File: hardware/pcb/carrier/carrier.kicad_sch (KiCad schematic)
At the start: 34 parts

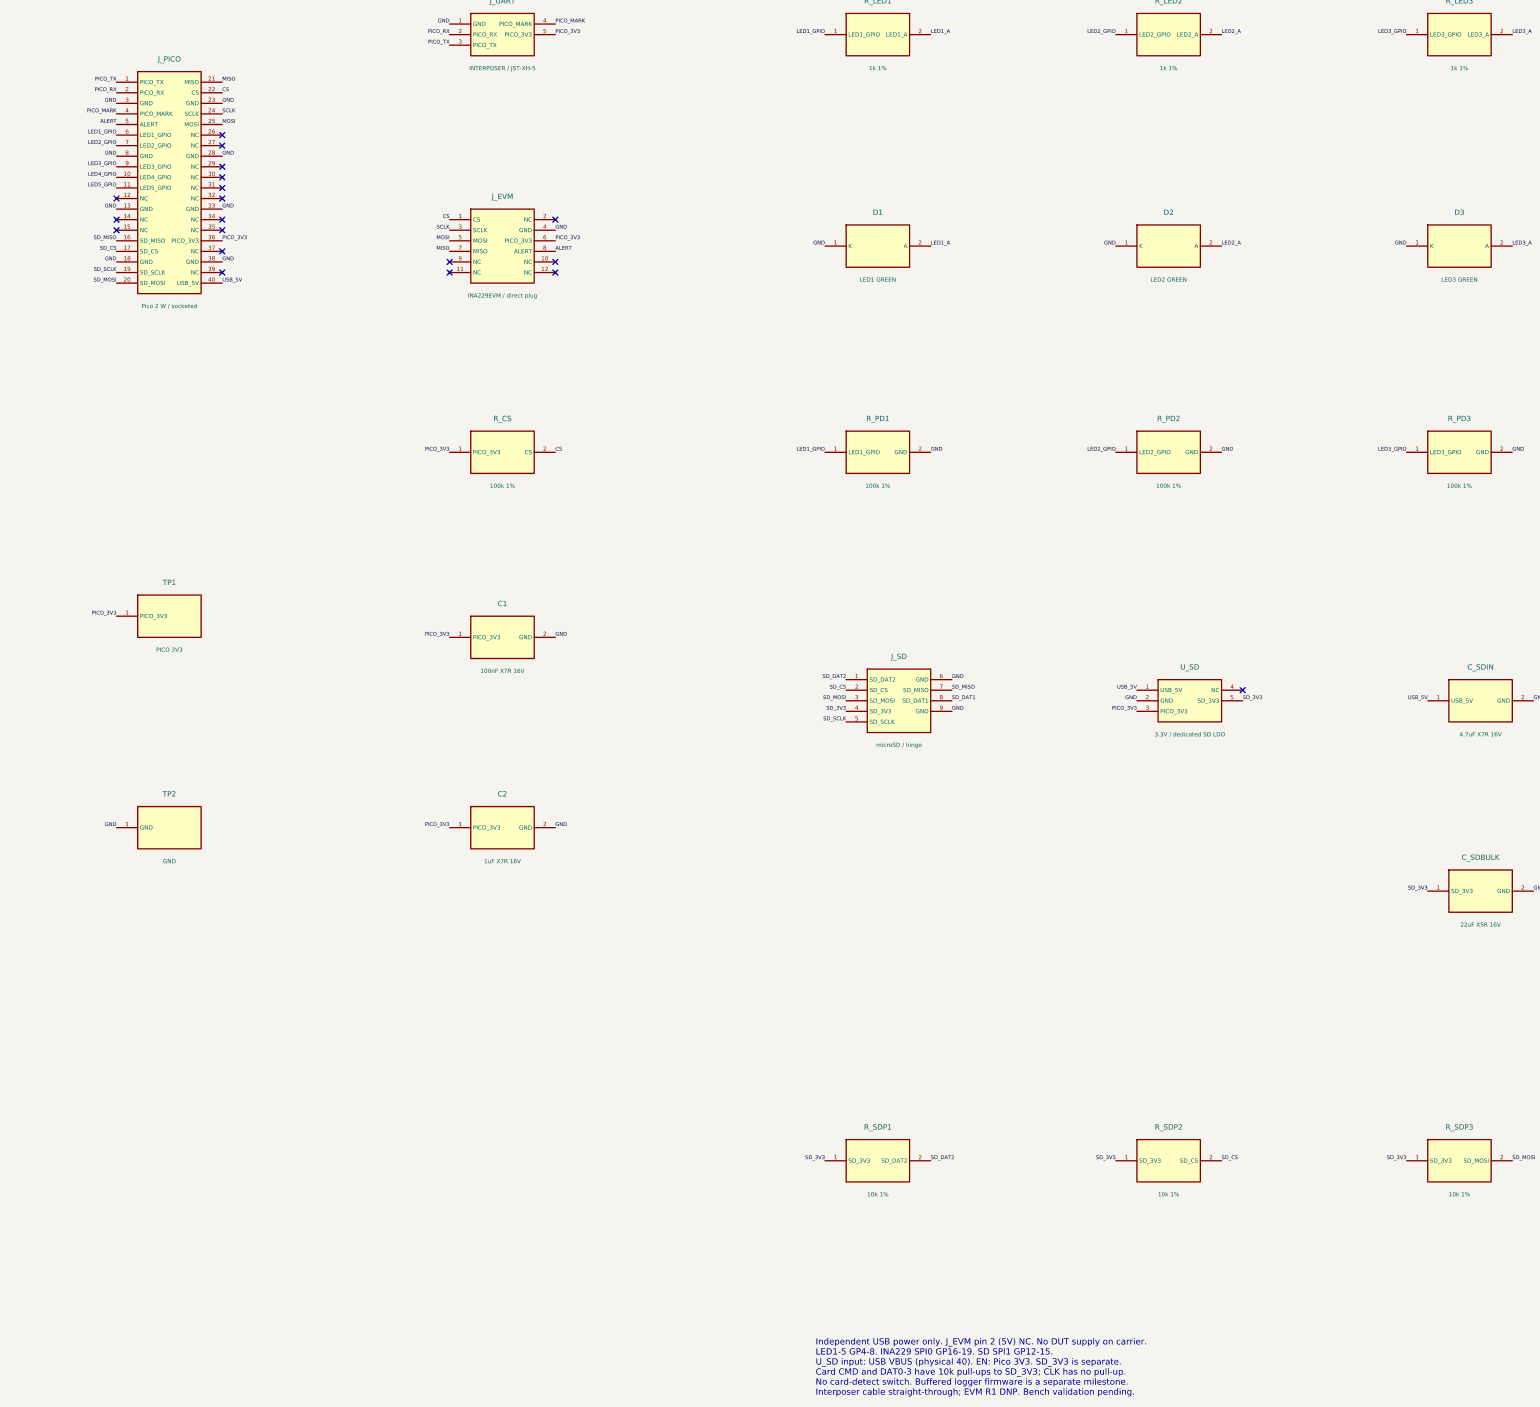
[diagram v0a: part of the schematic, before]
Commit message: Replace INA229EVM with an on-board INA229 on the carrier
- Carrier carries U_PM (INA229AIDGSR, VSSOP-10), 100 nF bypass, ALERT
  pull-up and a JST-XH sense connector J_SENSE (same pinout as interposer
  J3); the EVM socket and its footprint are removed.
- Carrier outline grows from 66 to 78 x 54 mm to make room.
- INA229 SPI0 moves to GP4-GP7 and the LEDs to GP27/26/22/21/20 so no
  trace crosses the Pico; ALERT stays on GP3.
- Carrier PWR_FLAGs added; source checks and tests updated for the new
  measurement boundary (sense nets only on J_SENSE and U_PM).
- BOM, assembly review, passive selections, checklist (new sense-ic row,
  carrier mock-up reset to pending), footprint review and docs updated.
- INA229 pad geometry compared with the TI DGS0010A example land pattern.
- Add project-state handoff note. Interposer and carrier fabrication
  gates remain open; nothing is released.

make carrier-build does not currently reproduce the routed board; the saved
carrier.kicad_pcb is the source of truth (see the carrier README).

Co-Authored-By: Claude Sonnet 5.5 <noreply@anthropic.com>
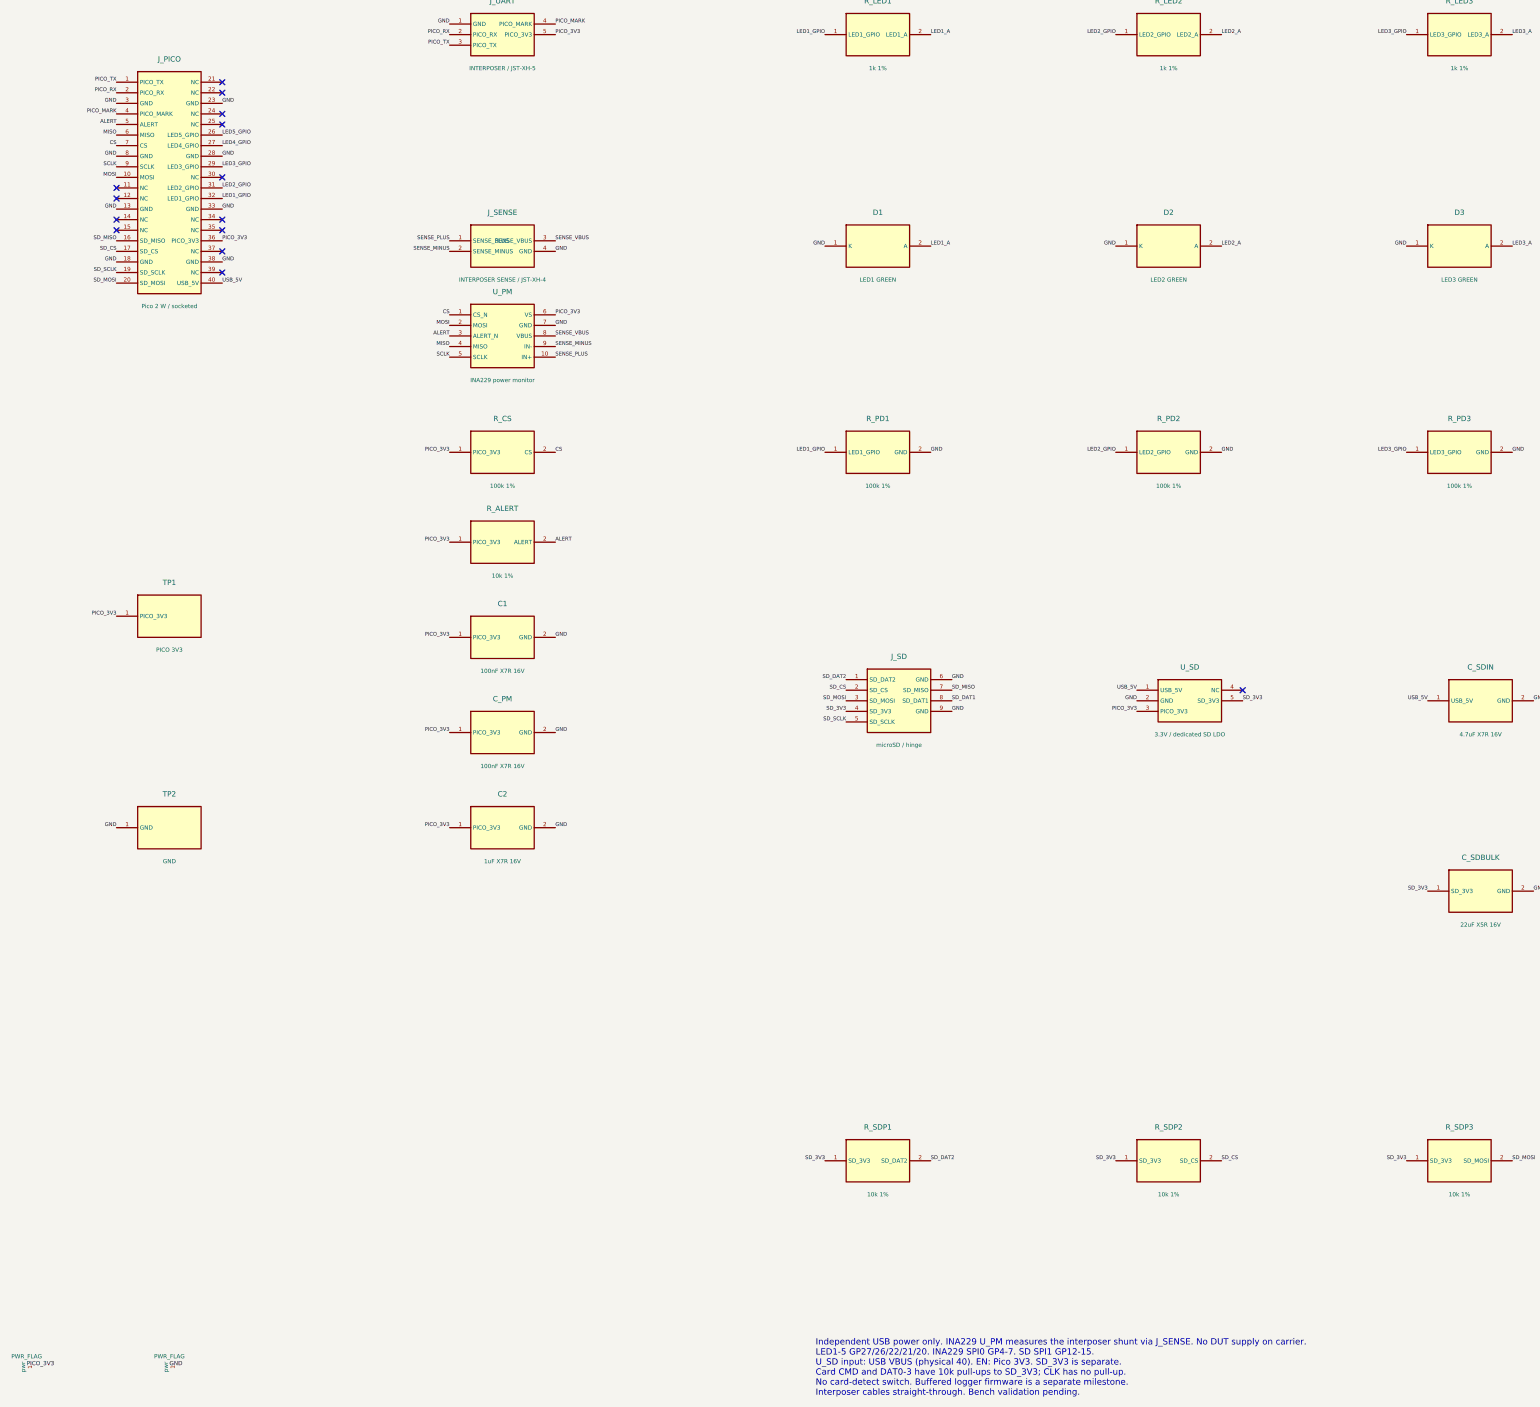
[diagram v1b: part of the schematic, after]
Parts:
- removed J_EVM: INA229EVM / direct plug, Carrier:NPPN062FJFN, symbol Carrier:J_EVM
- added C_PM: 100nF X7R 16V, Carrier:C_0805_Murata, symbol Carrier:C_PM
- added J_SENSE: INTERPOSER SENSE / JST-XH-4, Carrier:XH4, symbol Carrier:J_SENSE
- added R_ALERT: 10k 1%, Carrier:R_0805, symbol Carrier:R_ALERT
- added U_PM: INA229 power monitor, Carrier:VSSOP10, symbol Carrier:U_PM
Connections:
- net ALERT: now also R_ALERT.2 (ALERT), U_PM.3 (ALERT_N)
- net CS: now also J_PICO.7 (CS), U_PM.1 (CS_N); no longer J_PICO.22 (CS)
- net GND: now also C_PM.2 (GND), J_SENSE.4 (GND), U_PM.7 (GND)
- net LED1_GPIO: now also J_PICO.32 (LED1_GPIO); no longer J_PICO.6 (LED1_GPIO)
- net LED2_GPIO: now also J_PICO.31 (LED2_GPIO); no longer J_PICO.7 (LED2_GPIO)
- net LED3_GPIO: now also J_PICO.29 (LED3_GPIO); no longer J_PICO.9 (LED3_GPIO)
- net LED4_GPIO: now also J_PICO.27 (LED4_GPIO); no longer J_PICO.10 (LED4_GPIO)
- net LED5_GPIO: now also J_PICO.26 (LED5_GPIO); no longer J_PICO.11 (LED5_GPIO)
- net MISO: now also J_PICO.6 (MISO), U_PM.4 (MISO); no longer J_PICO.21 (MISO)
- net MOSI: now also J_PICO.10 (MOSI), U_PM.2 (MOSI); no longer J_PICO.25 (MOSI)
- net PICO_3V3: now also C_PM.1 (PICO_3V3), R_ALERT.1 (PICO_3V3), U_PM.6 (VS)
- net SCLK: now also J_PICO.9 (SCLK), U_PM.5 (SCLK); no longer J_PICO.24 (SCLK)
- new net SENSE_MINUS: J_SENSE.2 (SENSE_MINUS), U_PM.9 (IN-)
- new net SENSE_PLUS: J_SENSE.1 (SENSE_PLUS), U_PM.10 (IN+)
- new net SENSE_VBUS: J_SENSE.3 (SENSE_VBUS), U_PM.8 (VBUS)
- no-connect marks 19 -> 14
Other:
- note added: "Independent USB power only. INA229 U_PM measures the interposer shunt via J_SENSE. No DUT supply on carrier. LED1-5 GP27/26/22/21/20. INA229 SPI0 GP4-7. SD SPI1 GP12-15. U_SD input: USB VBUS (physical 40). EN: Pico 3V3. SD_3V3 is separate. Card CMD and DAT0-3 have 10k pull-ups to SD_3V3; CLK has no pull-up. No card-detect switch. Buffered logger firmware is a separate milestone. Interposer cables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"
- note removed: "Independent USB power only. J_EVM pin 2 (5V) NC. No DUT supply on carrier. LED1-5 GP4-8. INA229 SPI0 GP16-19. SD SPI1 GP12-15. U_SD input: USB VBUS (physical 40). EN: Pico 3V3. SD_3V3 is separate. Card CMD and DAT0-3 have 10k pull-ups to SD_3V3; CLK has no pull-up. No card-detect switch. Buffered logger firmware is a separate milestone. Interposer cable straight-through; EVM R1 DNP. Bench validat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"
